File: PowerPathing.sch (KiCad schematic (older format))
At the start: 15 parts

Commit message: Schematic Updates
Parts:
- added D?: 1N4001G, symbol Device:D
- added Q?: BSC026NE2LS5ATMA1, BSC026NE2LS5ATMA1, symbol Capstone:BSC026NE2LS5ATMA1
- added R?: 111 ohms, symbol Device:R
- added TP?: TestPoint - 12V Reg, symbol Connector:TestPoint
- added TP?: TestPoint - 5V Reg, symbol Connector:TestPoint
- added TP?: TestPoint - Power Circuit Out, symbol Connector:TestPoint
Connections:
- net labels added: 12V_Reg, 5V_Reg, Rechargeable_Batteries, VCC
- net labels removed: VCC_12, VIN_5V
- wire segments 70 -> 106
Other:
- moved on the sheet: C?, D?, IC?, L?, R?

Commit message: Schematic Updates, still need component values for driver circuit and keypad connector EDA
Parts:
- added TP?: GND 5V Reg, symbol Connector:TestPoint
- added TP?: GND 12V Reg, symbol Connector:TestPoint
- Q?: symbol Capstone:BSC026NE2LS5ATMA1 -> BoosterPack-rescue:BSC026NE2LS5ATMA1-Capstone-BoosterPack-rescue
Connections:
- net labels added: VS
- net labels removed: 12V_Reg
- wire segments 106 -> 108
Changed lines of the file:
@@
 5V_Reg
 Text HLabel 4050 5050 0    50   Output ~ 0
-12V_Reg
+VS
 $Comp
 L Connector:TestPoint TP?
@@
 	3600 1750 4000 1750
 $Comp
-L Capstone:BSC026NE2LS5ATMA1 Q?
+L BoosterPack-rescue:BSC026NE2LS5ATMA1-Capstone-BoosterPack-rescue Q?
 U 1 1 6164A765
 P 1950 3450
+AR Path="/6164A765" Ref="Q?"  Part="1"
+AR Path="/6153BBA2/6164A765" Ref="Q?"  Part="1"
 F 0 "Q?" H 2450 3715 50  0000 C CNN
 F 1 "BSC026NE2LS5ATMA1" H 2450 3624 50  0000 C CNN
@@
 L power:GND #PWR?
 U 1 1 616C1223
-P 7200 3000
-F 0 "#PWR?" H 7200 2750 50  0001 C CNN
-F 1 "GND" H 7205 2827 50  0000 C CNN
-F 2 "" H 7200 3000 50  0001 C CNN
-F 3 "" H 7200 3000 50  0001 C CNN
-	1    7200 3000
+P 7350 3000
+F 0 "#PWR?" H 7350 2750 50  0001 C CNN
+F 1 "GND" H 7355 2827 50  0000 C CNN
+F 2 "" H 7350 3000 50  0001 C CNN
+F 3 "" H 7350 3000 50  0001 C CNN
+	1    7350 3000
 	0    -1   -1   0
 $EndComp
-Wire Wire Line
-	7200 3000 7100 3000
 $Comp
 L power:GND #PWR?
@@
 Wire Wire Line
 	6750 4950 6900 4950
+Wire Wire Line
+	7100 3000 7350 3000
+$Comp
+L Connector:TestPoint TP?
+U 1 1 6184DFD4
+P 7200 3250
+AR Path="/61536750/6184DFD4" Ref="TP?"  Part="1"
+AR Path="/6153BBA2/6184DFD4" Ref="TP?"  Part="1"
+F 0 "TP?" H 7000 3400 50  0000 L CNN
+F 1 "GND 5V Reg" H 6800 3500 50  0000 L CNN
+F 2 "" H 7400 3250 50  0001 C CNN
+F 3 "~" H 7400 3250 50  0001 C CNN
+	1    7200 3250
+	-1   0    0    1
+$EndComp
+Wire Wire Line
+	7200 3250 7200 3000
+$Comp
+L Connector:TestPoint TP?
+U 1 1 61852063
+P 7150 5150
+AR Path="/61536750/61852063" Ref="TP?"  Part="1"
+AR Path="/6153BBA2/61852063" Ref="TP?"  Part="1"
+F 0 "TP?" V 7104 5338 50  0000 L CNN
+F 1 "GND 12V Reg" V 7195 5338 50  0000 L CNN
+F 2 "" H 7350 5150 50  0001 C CNN
+F 3 "~" H 7350 5150 50  0001 C CNN
+	1    7150 5150
+	0    1    1    0
+$EndComp
+Wire Wire Line
+	7150 5150 6900 5150
 $EndSCHEMATC

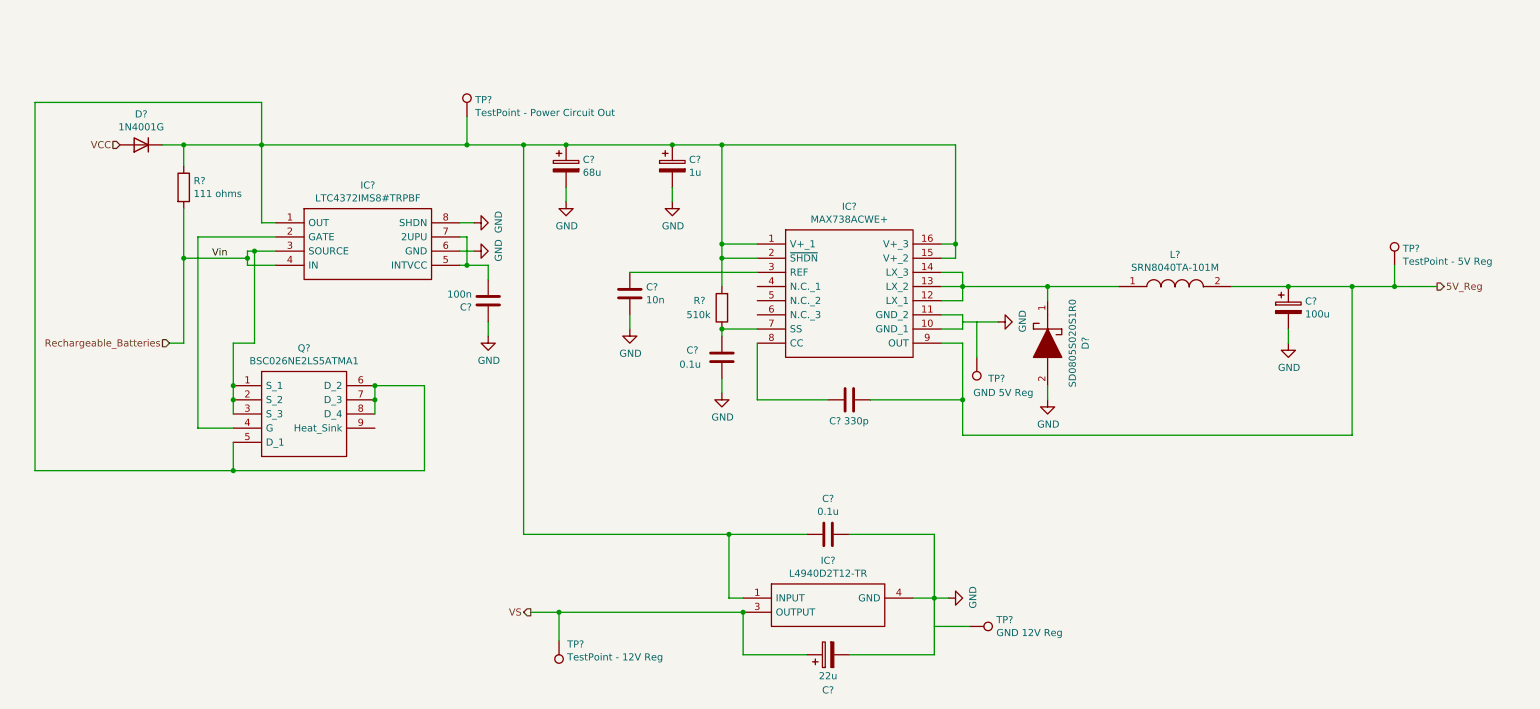
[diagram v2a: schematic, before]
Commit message: Added Generic Keypad Connector, don't know if we can use it or not
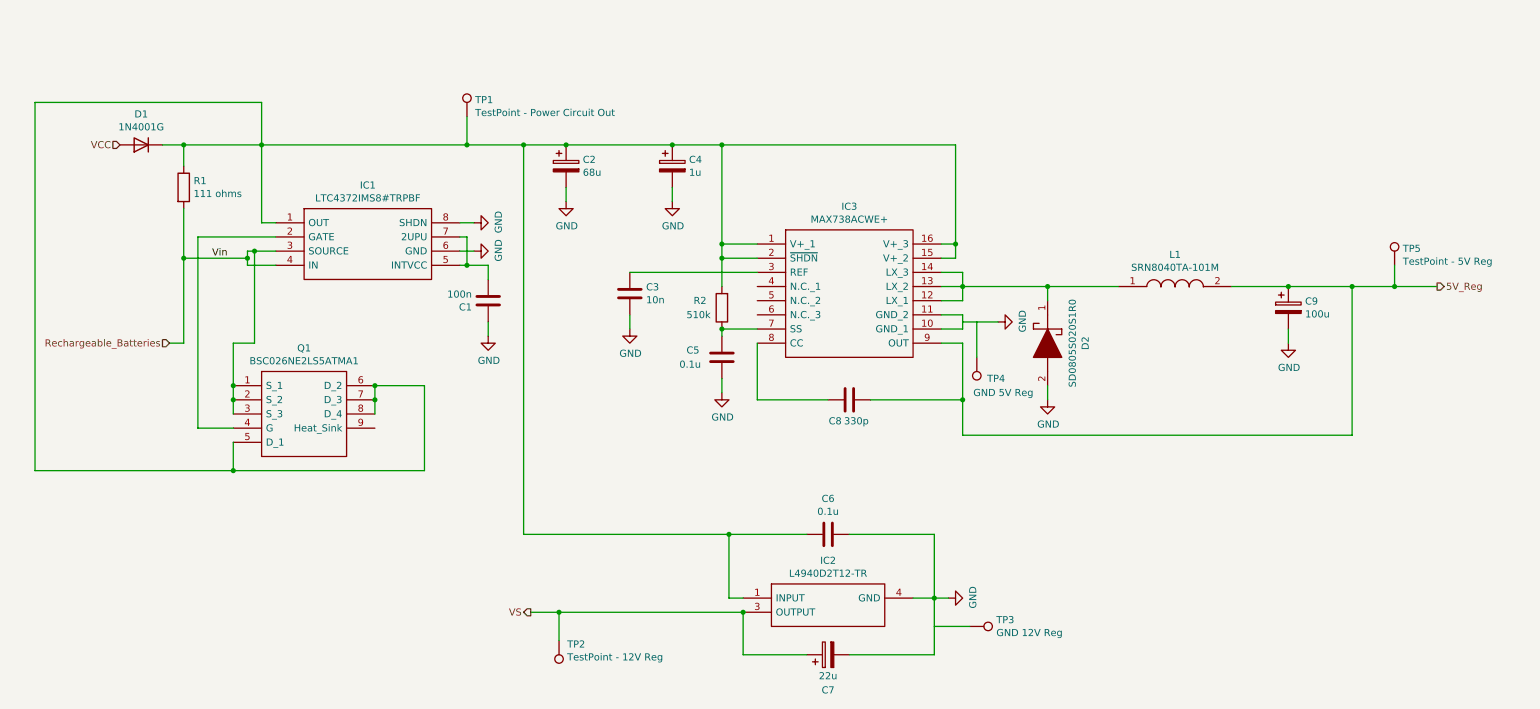
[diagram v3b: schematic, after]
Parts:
- gave numbers to parts that had none: 23
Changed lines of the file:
@@
 $EndDescr
 $Comp
-L Capstone:MAX738ACWE+ IC?
+L Capstone:MAX738ACWE+ IC3
 U 1 1 6153C30A
 P 5650 2450
-F 0 "IC?" H 6300 2715 50  0000 C CNN
+F 0 "IC3" H 6300 2715 50  0000 C CNN
 F 1 "MAX738ACWE+" H 6300 2624 50  0000 C CNN
 F 2 "SOIC127P1032X265-16N" H 6800 2550 50  0001 L CNN
@@
 $EndComp
 $Comp
-L Capstone:L4940D2T12-TR IC?
+L Capstone:L4940D2T12-TR IC2
 U 1 1 6153E2DB
 P 5550 4950
-F 0 "IC?" H 6150 5215 50  0000 C CNN
+F 0 "IC2" H 6150 5215 50  0000 C CNN
 F 1 "L4940D2T12-TR" H 6150 5124 50  0000 C CNN
 F 2 "TO254P1542X460-3N" H 6600 5050 50  0001 L CNN
@@
 $EndComp
 $Comp
-L Device:CP C?
+L Device:CP C9
 U 1 1 61548B4E
 P 9400 2900
-F 0 "C?" H 9518 2946 50  0000 L CNN
+F 0 "C9" H 9518 2946 50  0000 L CNN
 F 1 "100u" H 9518 2855 50  0000 L CNN
 F 2 "" H 9438 2750 50  0001 C CNN
@@
 $EndComp
 $Comp
-L Device:CP C?
+L Device:CP C4
 U 1 1 61549C3D
 P 5050 1900
-F 0 "C?" H 5168 1946 50  0000 L CNN
+F 0 "C4" H 5168 1946 50  0000 L CNN
 F 1 "1u" H 5168 1855 50  0000 L CNN
 F 2 "" H 5088 1750 50  0001 C CNN
@@
 Connection ~ 7050 2450
 $Comp
-L Device:C C?
+L Device:C C3
 U 1 1 6154C168
 P 4750 2800
-F 0 "C?" H 4865 2846 50  0000 L CNN
+F 0 "C3" H 4865 2846 50  0000 L CNN
 F 1 "10n" H 4865 2755 50  0000 L CNN
 F 2 "" H 4788 2650 50  0001 C CNN
@@
 	5650 2650 4750 2650
 $Comp
-L Device:R R?
+L Device:R R2
 U 1 1 6154CCF0
 P 5400 2900
-F 0 "R?" H 5600 2850 50  0000 R CNN
+F 0 "R2" H 5600 2850 50  0000 R CNN
 F 1 "510k" H 5650 2950 50  0000 R CNN
 F 2 "" V 5330 2900 50  0001 C CNN
@@
 	5400 3050 5650 3050
 $Comp
-L Device:C C?
+L Device:C C5
 U 1 1 6154DB48
 P 5400 3250
-F 0 "C?" H 5150 3300 50  0000 L CNN
+F 0 "C5" H 5150 3300 50  0000 L CNN
 F 1 "0.1u" H 5100 3200 50  0000 L CNN
 F 2 "" H 5438 3100 50  0001 C CNN
@@
 Connection ~ 5400 3050
 $Comp
-L Device:C C?
+L Device:C C8
 U 1 1 6154E910
 P 6300 3550
-F 0 "C?" V 6450 3450 50  0000 C CNN
+F 0 "C8" V 6450 3450 50  0000 C CNN
 F 1 "330p" V 6450 3600 50  0000 C CNN
 F 2 "" H 6338 3400 50  0001 C CNN
@@
 	6950 3050 7100 3050
 $Comp
-L Capstone:SD0805S020S1R0 D?
+L Capstone:SD0805S020S1R0 D2
 U 1 1 61551BA8
 P 7700 2750
-F 0 "D?" H 8100 3017 50  0000 C CNN
+F 0 "D2" H 8100 3017 50  0000 C CNN
 F 1 "SD0805S020S1R0" H 8100 2926 50  0000 C CNN
 F 2 "DIOM1613X100N" H 8200 2900 50  0001 L CNN
@@
 	7700 2750 8200 2750
 $Comp
-L Capstone:SRN8040TA-101M L?
+L Capstone:SRN8040TA-101M L1
 U 1 1 61561B3F
 P 8200 2750
-F 0 "L?" H 8600 2975 50  0000 C CNN
+F 0 "L1" H 8600 2975 50  0000 C CNN
 F 1 "SRN8040TA-101M" H 8600 2884 50  0000 C CNN
 F 2 "INDPM8080X450N" H 8850 2800 50  0001 L CNN
@@
 Connection ~ 9400 2750
 $Comp
-L Device:C C?
+L Device:C C6
 U 1 1 6156AEE8
 P 6150 4500
-F 0 "C?" V 5898 4500 50  0000 C CNN
+F 0 "C6" V 5898 4500 50  0000 C CNN
 F 1 "0.1u" V 5989 4500 50  0000 C CNN
 F 2 "" H 6188 4350 50  0001 C CNN
@@
 	5450 4500 6000 4500
 $Comp
-L Device:CP C?
+L Device:CP C7
 U 1 1 6156D3FC
 P 6150 5350
-F 0 "C?" V 5900 5350 50  0000 C CNN
+F 0 "C7" V 5900 5350 50  0000 C CNN
 F 1 "22u" V 6000 5350 50  0000 C CNN
 F 2 "" H 6188 5200 50  0001 C CNN
@@
 Connection ~ 5450 4500
 $Comp
-L Device:CP C?
+L Device:CP C2
 U 1 1 61572EC3
 P 4300 1900
-F 0 "C?" H 4418 1946 50  0000 L CNN
+F 0 "C2" H 4418 1946 50  0000 L CNN
 F 1 "68u" H 4418 1855 50  0000 L CNN
 F 2 "" H 4338 1750 50  0001 C CNN
@@
 	4300 1750 5050 1750
 $Comp
-L Capstone:LTC4372IMS8#TRPBF IC?
+L Capstone:LTC4372IMS8#TRPBF IC1
 U 1 1 6158EF55
 P 2250 2300
-F 0 "IC?" H 2900 2565 50  0000 C CNN
+F 0 "IC1" H 2900 2565 50  0000 C CNN
 F 1 "LTC4372IMS8#TRPBF" H 2900 2474 50  0000 C CNN
 F 2 "SOP65P490X110-8N" H 3400 2400 50  0001 L CNN
@@
 $EndComp
 $Comp
-L Device:C C?
+L Device:C C1
 U 1 1 615927B4
 P 3750 2850
-F 0 "C?" H 3865 2896 50  0000 L CNN
+F 0 "C1" H 3865 2896 50  0000 L CNN
 F 1 "100n" H 3865 2805 50  0000 L CNN
 F 2 "" H 3788 2700 50  0001 C CNN
@@
 Vin
 $Comp
-L Device:R R?
+L Device:R R1
 U 1 1 615CD244
 P 1600 2050
-F 0 "R?" H 1670 2096 50  0000 L CNN
+F 0 "R1" H 1670 2096 50  0000 L CNN
 F 1 "111 ohms" H 1670 2005 50  0000 L CNN
 F 2 "" V 1530 2050 50  0001 C CNN
@@
 $EndComp
 $Comp
-L Device:D D?
+L Device:D D1
 U 1 1 615CDA63
 P 1300 1750
-F 0 "D?" H 1300 1533 50  0000 C CNN
+F 0 "D1" H 1300 1533 50  0000 C CNN
 F 1 "1N4001G" H 1300 1624 50  0000 C CNN
 F 2 "" H 1300 1750 50  0001 C CNN
@@
 P 4250 5250
 AR Path="/61536750/6162E091" Ref="TP?"  Part="1"
-AR Path="/6153BBA2/6162E091" Ref="TP?"  Part="1"
-F 0 "TP?" H 4192 5276 50  0000 R CNN
+AR Path="/6153BBA2/6162E091" Ref="TP2"  Part="1"
+F 0 "TP2" H 4192 5276 50  0000 R CNN
 F 1 "TestPoint - 12V Reg" H 4192 5367 50  0000 R CNN
 F 2 "" H 4450 5250 50  0001 C CNN
@@
 P 10150 2600
 AR Path="/61536750/6163C53C" Ref="TP?"  Part="1"
-AR Path="/6153BBA2/6163C53C" Ref="TP?"  Part="1"
-F 0 "TP?" H 10208 2718 50  0000 L CNN
+AR Path="/6153BBA2/6163C53C" Ref="TP5"  Part="1"
+F 0 "TP5" H 10208 2718 50  0000 L CNN
 F 1 "TestPoint - 5V Reg" H 10208 2627 50  0000 L CNN
 F 2 "" H 10350 2600 50  0001 C CNN
@@
 P 3600 1550
 AR Path="/61536750/61644C04" Ref="TP?"  Part="1"
-AR Path="/6153BBA2/61644C04" Ref="TP?"  Part="1"
-F 0 "TP?" H 3658 1668 50  0000 L CNN
+AR Path="/6153BBA2/61644C04" Ref="TP1"  Part="1"
+F 0 "TP1" H 3658 1668 50  0000 L CNN
 F 1 "TestPoint - Power Circuit Out" H 3658 1577 50  0000 L CNN
 F 2 "" H 3800 1550 50  0001 C CNN
@@
 P 1950 3450
 AR Path="/6164A765" Ref="Q?"  Part="1"
-AR Path="/6153BBA2/6164A765" Ref="Q?"  Part="1"
-F 0 "Q?" H 2450 3715 50  0000 C CNN
+AR Path="/6153BBA2/6164A765" Ref="Q1"  Part="1"
+F 0 "Q1" H 2450 3715 50  0000 C CNN
 F 1 "BSC026NE2LS5ATMA1" H 2450 3624 50  0000 C CNN
 F 2 "BSC026NE2LS5ATMA1" H 2800 3550 50  0001 L CNN
@@
 Connection ~ 2950 3450
 $Comp
-L power:GND #PWR?
+L power:GND #PWR0101
 U 1 1 61689C6A
 P 3750 3100
-F 0 "#PWR?" H 3750 2850 50  0001 C CNN
+F 0 "#PWR0101" H 3750 2850 50  0001 C CNN
 F 1 "GND" H 3755 2927 50  0000 C CNN
 F 2 "" H 3750 3100 50  0001 C CNN
@@
 	3750 3100 3750 3000
 $Comp
-L power:GND #PWR?
+L power:GND #PWR0102
 U 1 1 6169BE0B
 P 3650 2300
-F 0 "#PWR?" H 3650 2050 50  0001 C CNN
+F 0 "#PWR0102" H 3650 2050 50  0001 C CNN
 F 1 "GND" H 3655 2127 50  0000 C CNN
 F 2 "" H 3650 2300 50  0001 C CNN
@@
 	3650 2300 3550 2300
 $Comp
-L power:GND #PWR?
+L power:GND #PWR0103
 U 1 1 6169F36F
 P 3650 2500
-F 0 "#PWR?" H 3650 2250 50  0001 C CNN
+F 0 "#PWR0103" H 3650 2250 50  0001 C CNN
 F 1 "GND" H 3655 2327 50  0000 C CNN
 F 2 "" H 3650 2500 50  0001 C CNN
@@
 	3650 2500 3550 2500
 $Comp
-L power:GND #PWR?
+L power:GND #PWR0104
 U 1 1 616A64FD
 P 4300 2150
-F 0 "#PWR?" H 4300 1900 50  0001 C CNN
+F 0 "#PWR0104" H 4300 1900 50  0001 C CNN
 F 1 "GND" H 4305 1977 50  0000 C CNN
 F 2 "" H 4300 2150 50  0001 C CNN
@@
 	4300 2150 4300 2050
 $Comp
-L power:GND #PWR?
+L power:GND #PWR0105
 U 1 1 616ACF0A
 P 5050 2150
-F 0 "#PWR?" H 5050 1900 50  0001 C CNN
+F 0 "#PWR0105" H 5050 1900 50  0001 C CNN
 F 1 "GND" H 5055 1977 50  0000 C CNN
 F 2 "" H 5050 2150 50  0001 C CNN
@@
 	5050 2150 5050 2050
 $Comp
-L power:GND #PWR?
+L power:GND #PWR0106
 U 1 1 616B3AEC
 P 4750 3050
-F 0 "#PWR?" H 4750 2800 50  0001 C CNN
+F 0 "#PWR0106" H 4750 2800 50  0001 C CNN
 F 1 "GND" H 4755 2877 50  0000 C CNN
 F 2 "" H 4750 3050 50  0001 C CNN
@@
 	4750 3050 4750 2950
 $Comp
-L power:GND #PWR?
+L power:GND #PWR0107
 U 1 1 616BA4E5
 P 5400 3500
-F 0 "#PWR?" H 5400 3250 50  0001 C CNN
+F 0 "#PWR0107" H 5400 3250 50  0001 C CNN
 F 1 "GND" H 5405 3327 50  0000 C CNN
 F 2 "" H 5400 3500 50  0001 C CNN
@@
 	7100 2950 7100 3050
 $Comp
-L power:GND #PWR?
+L power:GND #PWR0108
 U 1 1 616C1223
 P 7350 3000
-F 0 "#PWR?" H 7350 2750 50  0001 C CNN
+F 0 "#PWR0108" H 7350 2750 50  0001 C CNN
 F 1 "GND" H 7355 2827 50  0000 C CNN
 F 2 "" H 7350 3000 50  0001 C CNN
@@
 $EndComp
 $Comp
-L power:GND #PWR?
+L power:GND #PWR0109
 U 1 1 616C7A61
 P 9400 3150
-F 0 "#PWR?" H 9400 2900 50  0001 C CNN
+F 0 "#PWR0109" H 9400 2900 50  0001 C CNN
 F 1 "GND" H 9405 2977 50  0000 C CNN
 F 2 "" H 9400 3150 50  0001 C CNN
@@
 	9850 2750 9850 3800
 $Comp
-L power:GND #PWR?
+L power:GND #PWR0110
 U 1 1 616D8001
 P 7700 3550
-F 0 "#PWR?" H 7700 3300 50  0001 C CNN
+F 0 "#PWR0110" H 7700 3300 50  0001 C CNN
 F 1 "GND" H 7705 3377 50  0000 C CNN
 F 2 "" H 7700 3550 50  0001 C CNN
@@
 	7700 3550 7700 3450
 $Comp
-L power:GND #PWR?
+L power:GND #PWR0111
 U 1 1 616DE601
 P 7000 4950
-F 0 "#PWR?" H 7000 4700 50  0001 C CNN
+F 0 "#PWR0111" H 7000 4700 50  0001 C CNN
 F 1 "GND" H 7005 4777 50  0000 C CNN
 F 2 "" H 7000 4950 50  0001 C CNN
@@
 P 7200 3250
 AR Path="/61536750/6184DFD4" Ref="TP?"  Part="1"
-AR Path="/6153BBA2/6184DFD4" Ref="TP?"  Part="1"
-F 0 "TP?" H 7000 3400 50  0000 L CNN
+AR Path="/6153BBA2/6184DFD4" Ref="TP4"  Part="1"
+F 0 "TP4" H 7000 3400 50  0000 L CNN
 F 1 "GND 5V Reg" H 6800 3500 50  0000 L CNN
 F 2 "" H 7400 3250 50  0001 C CNN
@@
 P 7150 5150
 AR Path="/61536750/61852063" Ref="TP?"  Part="1"
-AR Path="/6153BBA2/61852063" Ref="TP?"  Part="1"
-F 0 "TP?" V 7104 5338 50  0000 L CNN
+AR Path="/6153BBA2/61852063" Ref="TP3"  Part="1"
+F 0 "TP3" V 7104 5338 50  0000 L CNN
 F 1 "GND 12V Reg" V 7195 5338 50  0000 L CNN
 F 2 "" H 7350 5150 50  0001 C CNN

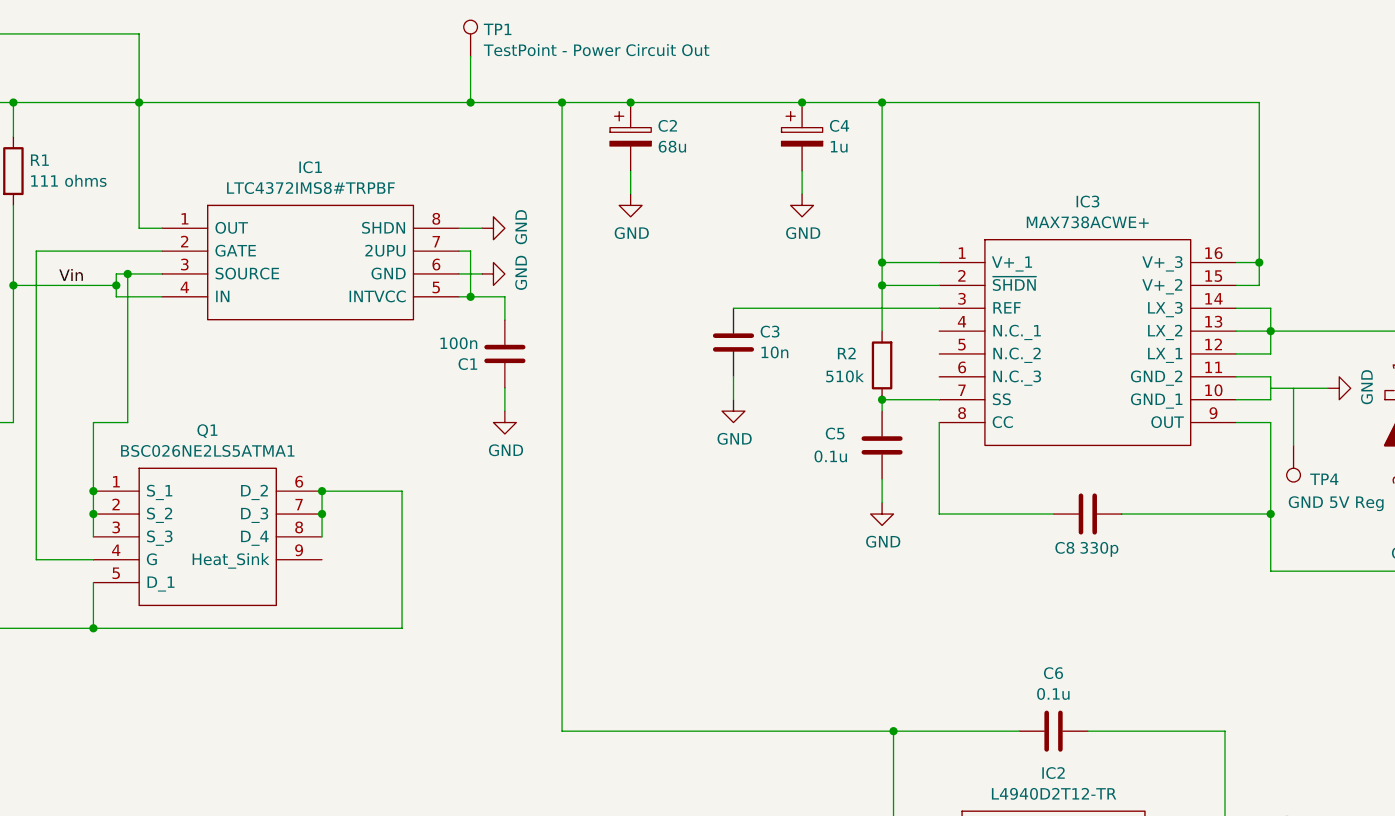
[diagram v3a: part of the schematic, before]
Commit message: Added labels for ease of reading and reorganized a sheet, still have a Generic Keypad Connector, don't know if we can use it or not
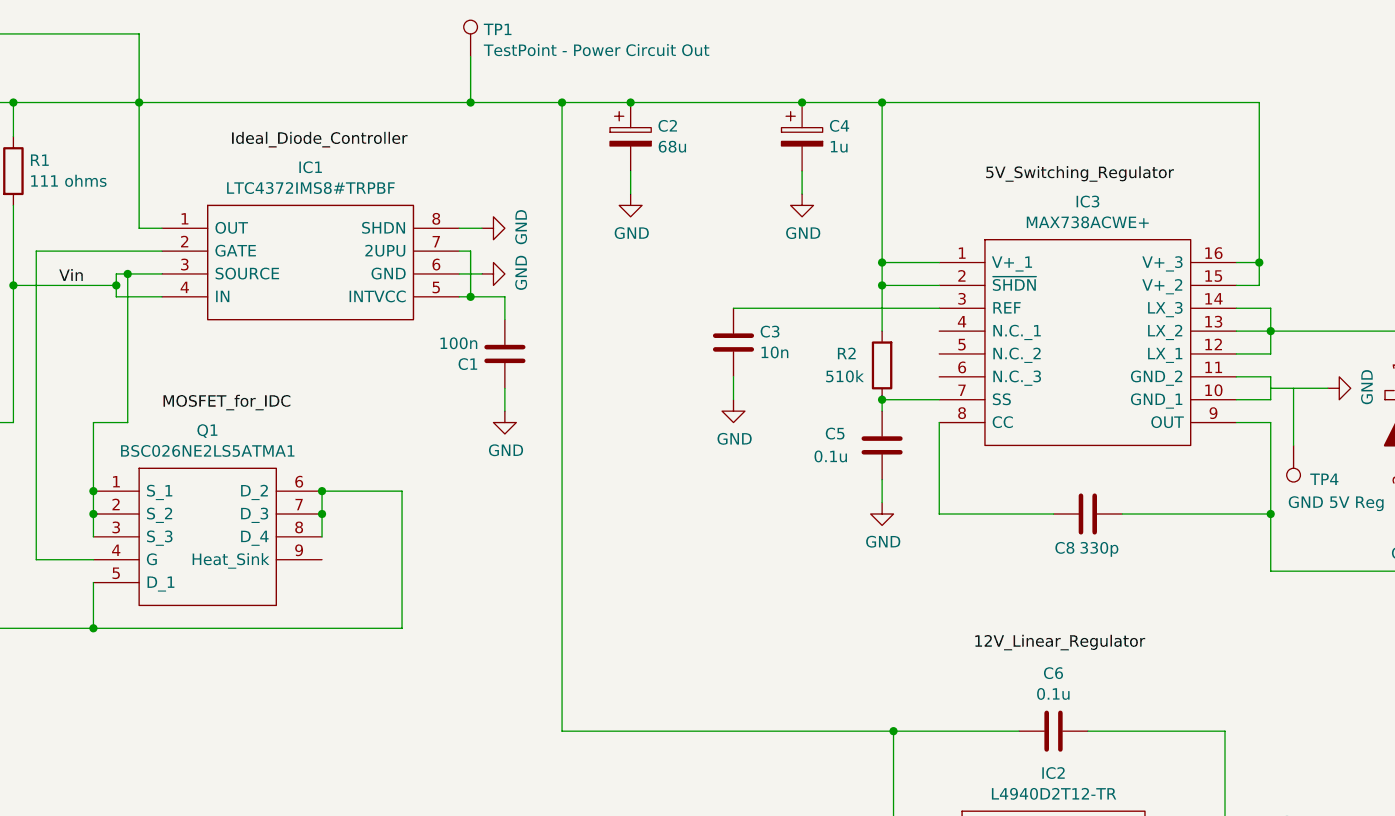
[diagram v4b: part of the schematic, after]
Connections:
- net labels added: 12V_Linear_Regulator, 5V_Switching_Regulator, Ideal_Diode_Controller, MOSFET_for_IDC
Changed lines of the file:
@@
 Wire Wire Line
 	7150 5150 6900 5150
+Text Label 5850 2100 0    50   ~ 0
+5V_Switching_Regulator
+Text Label 5800 4150 0    50   ~ 0
+12V_Linear_Regulator
+Text Label 2550 1950 0    50   ~ 0
+Ideal_Diode_Controller
+Text Label 2250 3100 0    50   ~ 0
+MOSFET_for_IDC
 $EndSCHEMATC
